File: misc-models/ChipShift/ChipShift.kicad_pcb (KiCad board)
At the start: 2 copper layers, 47 x 55.9 mm, 3 parts, among them J1 Conn_01x40, J2 Conn_01x40, J3 Conn_01x40

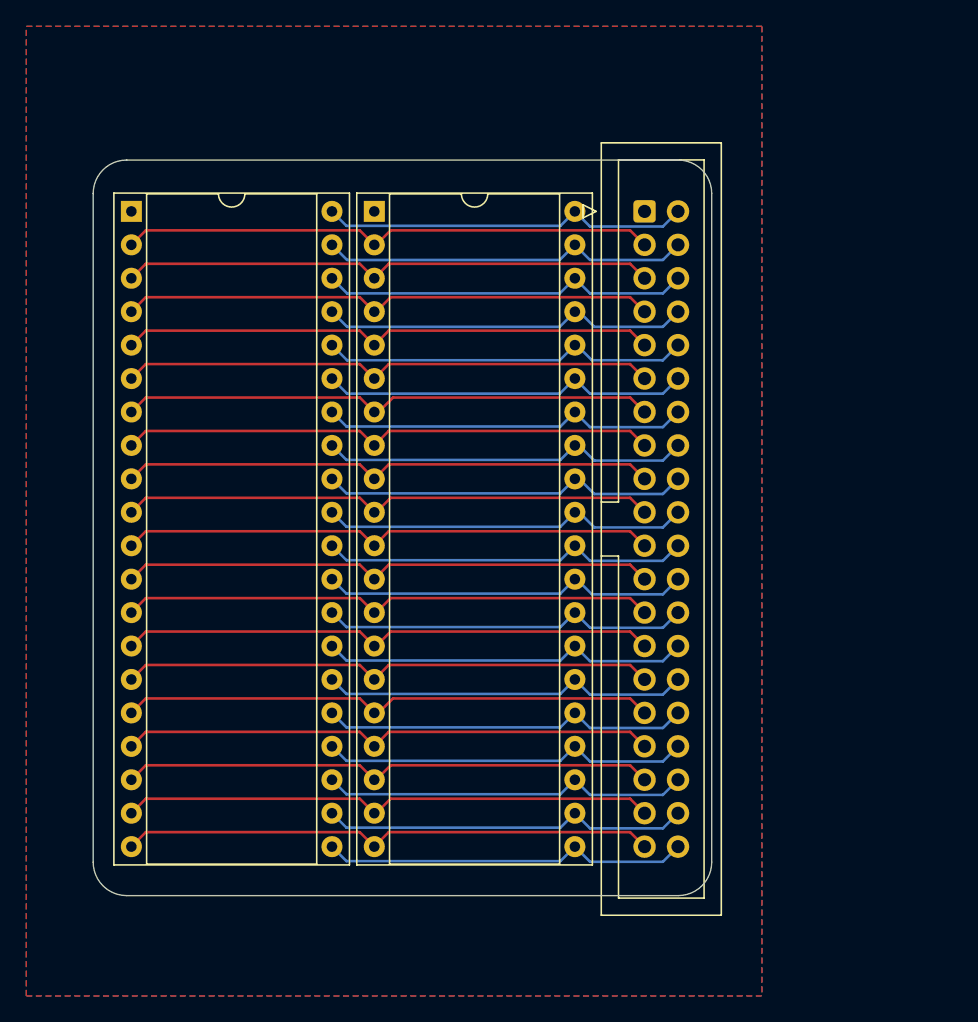
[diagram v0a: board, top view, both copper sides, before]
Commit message: Chip breakout boards use larger holes to allow for precision sockets to go through
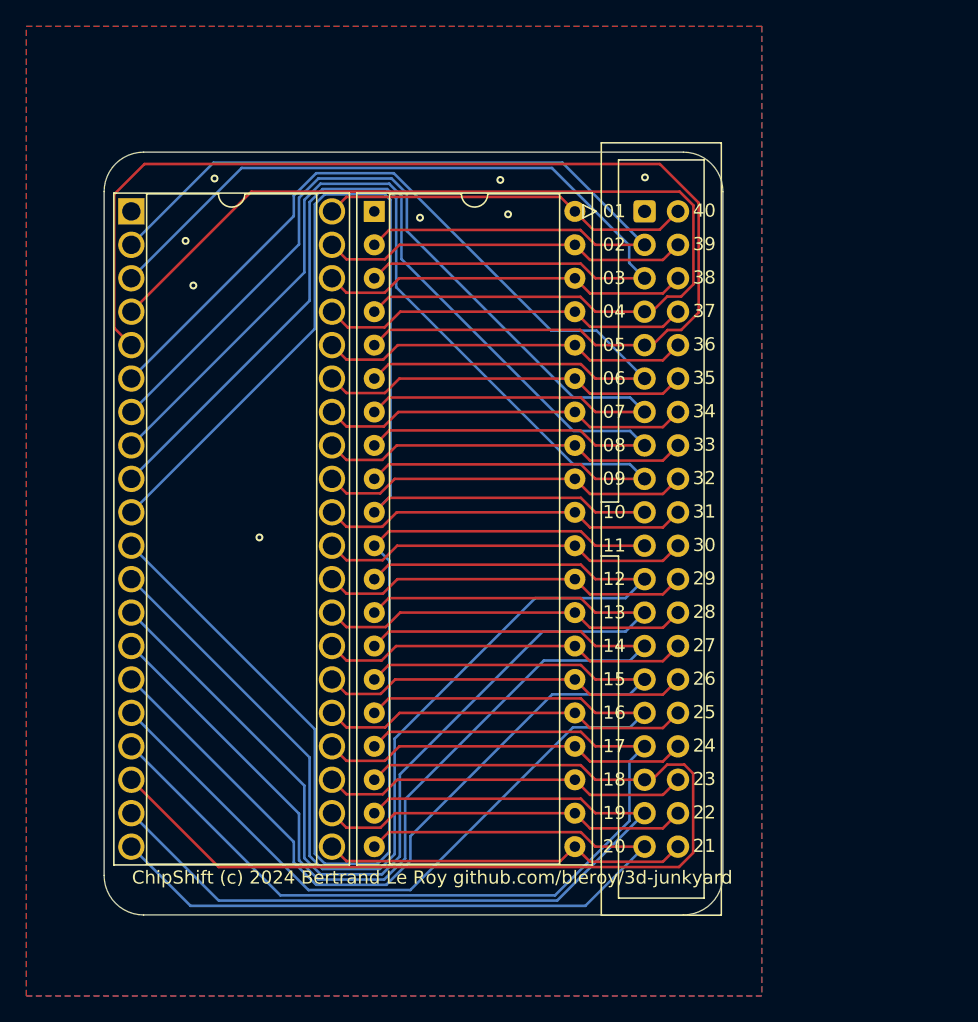
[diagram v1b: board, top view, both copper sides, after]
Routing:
- net Net-(J1-Pin_5): track 40.8 -> 92.9 mm
- net Net-(J1-Pin_12): track 40.8 -> 88.2 mm
- net Net-(J1-Pin_9): track 40.8 -> 87.0 mm
- net Net-(J1-Pin_13): track 40.8 -> 83.8 mm
- net Net-(J1-Pin_8): track 40.8 -> 83.0 mm
- net Net-(J1-Pin_10): track 40.8 -> 81.1 mm
- net Net-(J1-Pin_11): track 40.8 -> 80.7 mm
- net Net-(J1-Pin_14): track 40.8 -> 79.8 mm
- net Net-(J1-Pin_7): track 40.8 -> 78.9 mm
- net Net-(J1-Pin_4): track 40.8 -> 78.4 mm
- net Net-(J1-Pin_18): track 40.8 -> 77.2 mm
- net Net-(J1-Pin_15): track 40.8 -> 75.4 mm
- net Net-(J1-Pin_6): track 40.8 -> 74.3 mm
- net Net-(J1-Pin_17): track 40.8 -> 72.5 mm
- net Net-(J1-Pin_16): track 40.8 -> 71.6 mm
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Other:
- board size 47 x 55.9 mm -> 47 x 58 mm
